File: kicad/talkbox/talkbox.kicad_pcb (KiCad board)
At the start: 2 copper layers, 89 x 46 mm, 43 parts, among them J1 AudioJack2, J2 Conn_02x04_Odd_Even, J3 AudioJack2, J4 Barrel_Jack_Switch, SW1 SW_SPST, U1 TL071, U2 SW_3PDT, U4 LT1054xSOIC16, U5 LM7812_TO220, U6 LM7912_TO220, U7 logo

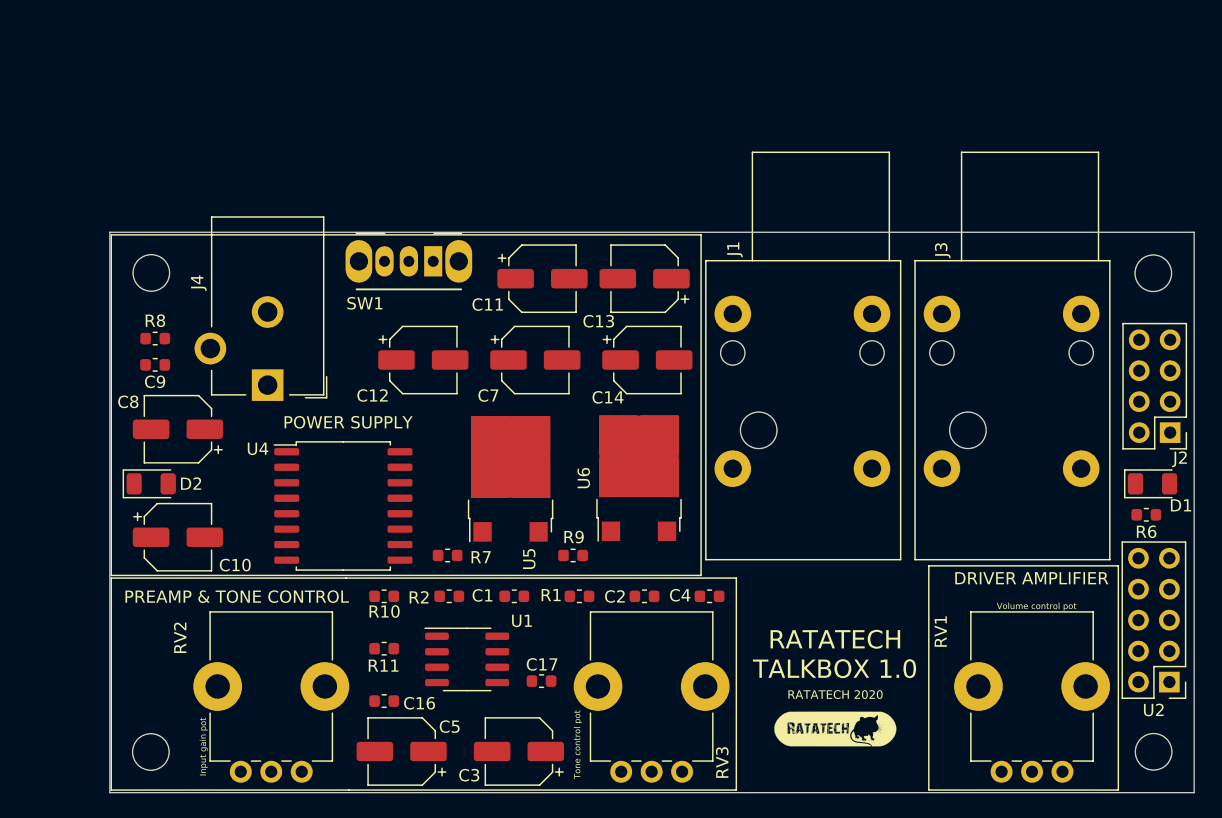
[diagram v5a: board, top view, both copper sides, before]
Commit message: Changed preamp capacitors to electrolytics
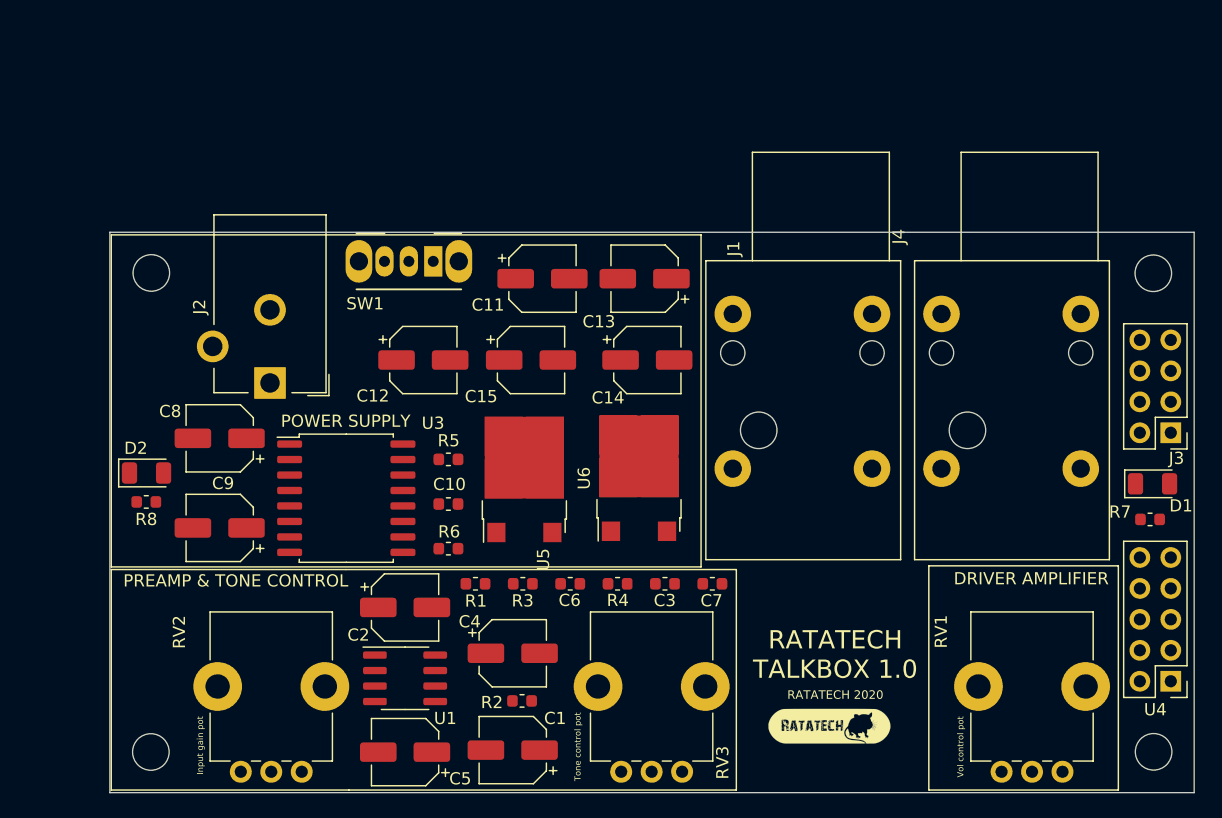
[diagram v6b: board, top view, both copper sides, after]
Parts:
- removed C16, C17: 10uF, Capacitor_SMD:C_0603_1608Metric
- removed R10: 1000k, Resistor_SMD:R_0603_1608Metric
- removed R11: 2k, Resistor_SMD:R_0603_1608Metric
- removed R9: 470, Resistor_SMD:R_0603_1608Metric
- removed U7: logo, imgs:ratatech_bitmap_10x2.8mm
- added C15: 1uF, Capacitor_SMD:CP_Elec_5x5.3, F.Cu at (118.2, 84.5)
- added C6: 4.7nF, Capacitor_SMD:C_0603_1608Metric, F.Cu at (121.4, 102.8)
- added R3: 9.1K, Resistor_SMD:R_0603_1608Metric, F.Cu at (117.5, 102.8)
- added R4: 9.1K, Resistor_SMD:R_0603_1608Metric, F.Cu at (125.3, 102.8)
- added R5: 22K, Resistor_SMD:R_0603_1608Metric, F.Cu at (111.4, 92.6)
- added U3: LT1054xSOIC16, Package_SO:SOIC-16W_7.5x10.3mm_P1.27mm, F.Cu at (103.0, 95.8)
- C1, C2: value 4.7nF -> 10uF; footprint Capacitor_SMD:C_0603_1608Metric -> Capacitor_SMD:CP_Elec_5x5.3
- C10: value 100uF -> 0.002uF; footprint Capacitor_SMD:CP_Elec_5x5.3 -> Capacitor_SMD:C_0603_1608Metric
- C11: value 2uF -> 100uF
- C13: value 1uF -> 2uF
- C3: value 100uF -> 22pF; footprint Capacitor_SMD:CP_Elec_5x5.3 -> Capacitor_SMD:C_0603_1608Metric
- C4: value 22pF -> 100uF; footprint Capacitor_SMD:C_0603_1608Metric -> Capacitor_SMD:CP_Elec_5x5.3
- C7: value 2uF -> 4.7nF; footprint Capacitor_SMD:CP_Elec_5x5.3 -> Capacitor_SMD:C_0603_1608Metric
- C8: value 10uF -> 2uF
- C9: value 0.002uF -> 10uF; footprint Capacitor_SMD:C_0603_1608Metric -> Capacitor_SMD:CP_Elec_5x5.3
- J2: value Conn_02x04_Odd_Even -> Barrel_Jack_Switch; footprint Connector_PinHeader_2.54mm:PinHeader_2x04_P2.54mm_Vertical -> Connector_BarrelJack:BarrelJack_CUI_PJ-102AH_Horizontal
- J3: value AudioJack2 -> Conn_02x04_Odd_Even; footprint Connector_Audio_Extended:Jack_6.35mm_Neutrik_NRJ4HF-1_Horizontal -> Connector_PinHeader_2.54mm:PinHeader_2x04_P2.54mm_Vertical
- J4: value Barrel_Jack_Switch -> AudioJack2; footprint Connector_BarrelJack:BarrelJack_CUI_PJ-102AH_Horizontal -> Connector_Audio_Extended:Jack_6.35mm_Neutrik_NRJ4HF-1_Horizontal
- R1: value 9.1K -> 1000k
- R2: value 9.1K -> 2k
- R6: value 470 -> 240K
- R7: value 22K -> 470
- R8: value 240K -> 470
- U2: value SW_3PDT -> logo; footprint Connector_PinHeader_2.54mm:PinHeader_2x05_P2.54mm_Vertical -> imgs:ratatech_bitmap_10x2.8mm
- U4: value LT1054xSOIC16 -> SW_3PDT; footprint Package_SO:SOIC-16W_7.5x10.3mm_P1.27mm -> Connector_PinHeader_2.54mm:PinHeader_2x05_P2.54mm_Vertical
- moved J2 74.6 mm to (96.7, 80.3)
- moved U4 69.4 mm to (170.7, 110.8), turned to 180 degrees
- moved R7 57.7 mm to (169.0, 97.6), turned to 180 degrees
- moved R6 57.4 mm to (111.4, 100.0)
- moved J4 55.3 mm to (151.9, 80.7), turned to 90 degrees
- moved U2 28.1 mm to (142.7, 114.5), turned to 0 degrees
- moved C7 23.4 mm to (133.0, 102.8)
- moved C10 22.4 mm to (111.4, 96.3)
- moved J3 20.9 mm to (170.7, 90.4), turned to 180 degrees
- moved C2 19.7 mm to (107.8, 104.8)
- moved C3 18.3 mm to (129.2, 102.8)
- moved C4 16.8 mm to (116.7, 108.5)
- moved C9 14.4 mm to (92.6, 98.3)
- moved R8 13.4 mm to (86.6, 96.1), turned to 180 degrees
- moved C1 12.6 mm to (116.7, 116.5)
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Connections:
- C10 pad 1: driver_- -> Net-(C10-Pad1)
- C11 pad 1: Net-(C11-Pad1) -> driver_-
- C11 pad 2: driver_- -> Net-(C10-Pad1)
- C12 pad 1: driver_- -> Net-(C12-Pad1)
- C12 pad 2: Net-(C10-Pad2) -> driver_-
- C13 pad 1: VCC -> driver_-
- C13 pad 2: driver_- -> Net-(C10-Pad1)
- C14 pad 1: driver_- -> VCC
- C14 pad 2: VDD -> driver_-
- C2 pad 1: (no net) -> input
- C3 pad 1: VCC -> preamp_output
- C3 pad 2: driver_- -> Net-(C3-Pad2)
- C4 pad 1: preamp_output -> driver_-
- C4 pad 2: Net-(C4-Pad2) -> VDD
- C5 pad 1: driver_- -> VCC
- C5 pad 2: VDD -> driver_-
- C7 pad 1: Net-(C11-Pad1) -> tone_control_output
- C7 pad 2: driver_- -> Net-(C7-Pad2)
- C8 pad 1: Net-(C8-Pad1) -> Net-(C12-Pad1)
- C8 pad 2: Net-(C8-Pad2) -> driver_-
- C9 pad 1: Net-(C10-Pad2) -> Net-(C9-Pad1)
- J2 pad 1: pa_input -> Net-(J2-Pad1)
- J2 pad 3: VCC -> driver_-
- R1 pad 1: Net-(C1-Pad1) -> driver_-
- R1 pad 2: preamp_output -> Net-(C2-Pad2)
- R2 pad 1: Net-(C4-Pad2) -> Net-(C1-Pad1)
- R2 pad 2: driver_- -> Net-(R2-Pad2)
- R6 pad 1: Net-(D1-Pad2) -> Net-(C10-Pad2)
- R6 pad 2: Net-(R6-Pad2) -> Net-(C10-Pad1)
- R7 pad 1: Net-(C9-Pad2) -> Net-(D1-Pad2)
- R8 pad 1: Net-(C9-Pad2) -> Net-(D2-Pad2)
- R8 pad 2: Net-(C10-Pad2) -> VCC
- RV1 pad 1: preamp_output -> Net-(C3-Pad2)
- RV1 pad 2: pa_input -> Net-(C7-Pad2)
- RV1 pad 3: driver_- -> Net-(C6-Pad1)
- RV2 pad 1: Net-(R11-Pad2) -> Net-(R2-Pad2)
- RV2 pad 2: Net-(R11-Pad2) -> Net-(R2-Pad2)
- RV3 pad 1: Net-(C4-Pad2) -> tone_control_output
- RV3 pad 2: Net-(C2-Pad2) -> pa_input
- RV3 pad 3: Net-(C1-Pad1) -> driver_-
- SW1 pad 1: Net-(J4-Pad1) -> Net-(J2-Pad1)
- SW1 pad 2: Net-(C11-Pad1) -> Net-(C12-Pad1)
- U1 pad 2: Net-(C17-Pad2) -> Net-(R2-Pad2)
- U1 pad 3: Net-(R11-Pad2) -> Net-(C2-Pad2)
- U4 pad 1: (no net) -> pa_output
- U4 pad 2: (no net) -> driver_+
- U4 pad 3: Net-(C9-Pad2) -> (no net)
- U4 pad 4: Net-(C8-Pad1) -> (no net)
- U4 pad 5: driver_- -> Net-(J4-PadT)
- U4 pad 6: Net-(C8-Pad2) -> input
- U4 pad 7: (no net) -> VCC
- U4 pad 8: (no net) -> Net-(R7-Pad2)
- U5 pad 1: Net-(C11-Pad1) -> Net-(C12-Pad1)
- U6 pad 2: Net-(C10-Pad2) -> Net-(C10-Pad1)
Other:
- board text added: "Vol control pot"
- board text added: "gnd"
- board text removed: "Volume control pot"

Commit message: Re-labeled drive- to GND
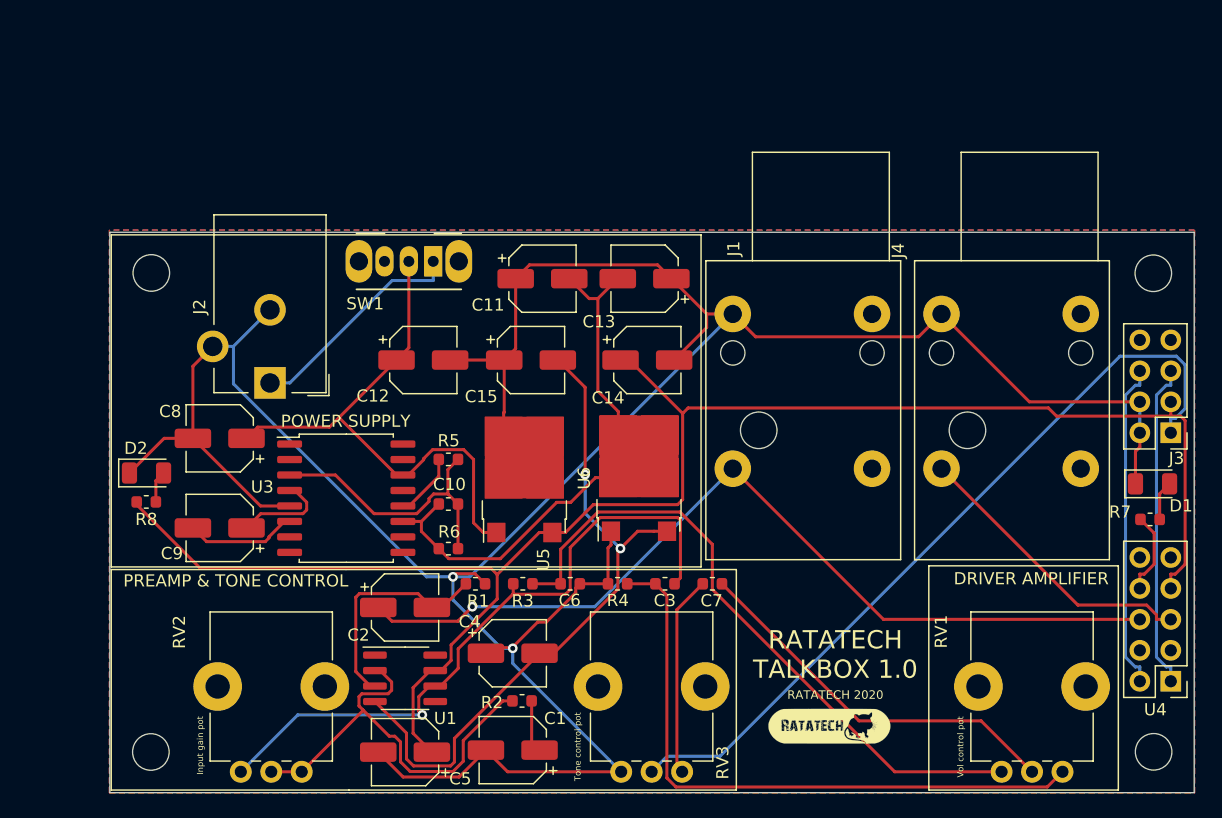
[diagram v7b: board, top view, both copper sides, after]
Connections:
- C1 pad 2: driver_- -> GND
- C11 pad 1: driver_- -> GND
- C12 pad 2: driver_- -> GND
- C13 pad 1: driver_- -> GND
- C14 pad 2: driver_- -> GND
- C15 pad 1: driver_- -> GND
- C4 pad 1: driver_- -> GND
- C5 pad 2: driver_- -> GND
- C6 pad 2: driver_- -> GND
- C8 pad 2: driver_- -> GND
- D1 pad 1: driver_- -> GND
- D2 pad 1: driver_- -> GND
- J1 pad S: driver_- -> GND
- J2 pad 2: driver_- -> GND
- J2 pad 3: driver_- -> GND
- J3 pad 2: driver_- -> GND
- J3 pad 4: driver_- -> GND
- J3 pad 7: driver_- -> (no net)
- J4 pad S: driver_- -> GND
- R1 pad 1: driver_- -> GND
- R4 pad 2: driver_- -> GND
- RV3 pad 3: driver_- -> GND
- U3 pad 5: driver_- -> GND
- U5 pad 2: driver_- -> GND
- U6 pad 1: driver_- -> GND
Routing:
- net GND: track 0.00 -> 253.2 mm, vias 0 -> 2
- net VCC: track 0.00 -> 140.1 mm
- net input: track 0.00 -> 73.3 mm, vias 0 -> 1
- net pa_input: track 0.00 -> 64.5 mm
- net VDD: track 0.00 -> 56.0 mm, vias 0 -> 2
- net preamp_output: track 0.00 -> 55.3 mm, vias 0 -> 1
- net Net-(C6-Pad1): track 0.00 -> 53.6 mm
- net Net-(C3-Pad2): track 0.00 -> 51.9 mm
- net Net-(C10-Pad1): track 0.00 -> 51.9 mm
- net Net-(C12-Pad1): track 0.00 -> 45.1 mm
- net Net-(R2-Pad2): track 0.00 -> 34.9 mm
- net Net-(C7-Pad2): track 0.00 -> 31.8 mm
- net pa_output: track 0.00 -> 26.9 mm
- net driver_+: track 0.00 -> 26.9 mm
- net Net-(J4-PadT): track 0.00 -> 24.2 mm
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- added copper zone on B.Cu, net GND
- added copper zone on F.Cu, net GND
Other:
- board text removed: "driver-"

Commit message: PCB done v1.0. Generated gerbers for fab
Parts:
- C3: value 22pF -> 6.8nF
- C6: value 4.7nF -> 10nF
- C7: value 4.7nF -> 47nF
- R3: value 9.1K -> 47K
- R4: value 9.1K -> 22K
- RV1: value 10K -> 20K
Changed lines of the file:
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@@
     (pcbplotparams
       (layerselection 0x010fc_ffffffff)
-      (usegerberextensions false)
+      (usegerberextensions true)
       (usegerberattributes false)
       (usegerberadvancedattributes false)
@@
       (outputformat 1)
       (mirror false)
-      (drillshape 1)
+      (drillshape 0)
       (scaleselection 1)
-      (outputdirectory ""))
+      (outputdirectory "../gerber/"))
   )
   (net 0 "")
@@
     (add_net "Net-(D2-Pad2)")
     (add_net "Net-(J2-Pad1)")
+    (add_net "Net-(J3-Pad7)")
+    (add_net "Net-(J3-Pad8)")
     (add_net "Net-(J4-PadT)")
     (add_net "Net-(R2-Pad2)")
     (add_net "Net-(R5-Pad2)")
     (add_net "Net-(R7-Pad2)")
+    (add_net "Net-(U1-Pad1)")
+    (add_net "Net-(U1-Pad5)")
+    (add_net "Net-(U1-Pad8)")
+    (add_net "Net-(U3-Pad13)")
+    (add_net "Net-(U4-Pad3)")
+    (add_net "Net-(U4-Pad4)")
+    (add_net "Net-(U4-Pad9)")
     (add_net VCC)
     (add_net VDD)
@@
       (effects (font (size 1 1) (thickness 0.15)))
     )
-    (fp_text value 9.1K (at 0 1.43) (layer F.Fab)
+    (fp_text value 22K (at 0 1.43) (layer F.Fab)
       (effects (font (size 1 1) (thickness 0.15)))
     )
@@
       (effects (font (size 1 1) (thickness 0.15)))
     )
-    (fp_text value 9.1K (at 0 1.43) (layer F.Fab)
+    (fp_text value 47K (at 0 1.43) (layer F.Fab)
       (effects (font (size 1 1) (thickness 0.15)))
     )
@@
       (effects (font (size 1 1) (thickness 0.15)))
     )
-    (fp_text value 4.7nF (at 0 1.43) (layer F.Fab)
+    (fp_text value 47nF (at 0 1.43) (layer F.Fab)
       (effects (font (size 1 1) (thickness 0.15)))
     )
@@
       (effects (font (size 1 1) (thickness 0.15)))
     )
-    (fp_text value 4.7nF (at 0 1.43) (layer F.Fab)
+    (fp_text value 10nF (at 0 1.43) (layer F.Fab)
       (effects (font (size 1 1) (thickness 0.15)))
     )
@@
       (effects (font (size 1 1) (thickness 0.15)))
     )
-    (fp_text value 22pF (at 0 1.43) (layer F.Fab)
+    (fp_text value 6.8nF (at 0 1.43) (layer F.Fab)
       (effects (font (size 1 1) (thickness 0.15)))
     )
@@
       (effects (font (size 1 1) (thickness 0.15)))
     )
-    (fp_text value 10K (at 7.69 1.316 90) (layer F.Fab)
-      (effects (font (size 1 1) (thickness 0.15)))
-    )
+    (fp_text value 20K (at 7.69 1.316 90) (layer F.Fab)
+      (effects (font (size 1 1) (thickness 0.15)))
+    )
